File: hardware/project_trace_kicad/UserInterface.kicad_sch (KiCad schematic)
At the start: 13 parts, among them J4 Conn_01x07_Pin, J5 Conn_01x07_Socket, SW1 SW_Push, SW2 SW_Push, SW3 RotaryEncoder, SW4 RotaryEncoder, U1 SBC-OLED01.3

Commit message: Add missing Part-numers, Revise AC Coupling
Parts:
- R1, R2, R3, R4, R5, R6: DigikeyPN (none) -> YAG1236CT-ND
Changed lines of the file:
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@@
+			)
+		)
+		(property "DigikeyPN" "YAG1236CT-ND"
+			(at 195.58 90.17 0)
+			(hide yes)
+			(show_name no)
+			(do_not_autoplace no)
+			(effects
+				(font
+					(size 1.27 1.27)
+				)
 			)
 		)
@@
 			)
 		)
+		(property "DigikeyPN" "YAG1236CT-ND"
+			(at 210.82 115.57 0)
+			(hide yes)
+			(show_name no)
+			(do_not_autoplace no)
+			(effects
+				(font
+					(size 1.27 1.27)
+				)
+			)
+		)
 		(pin "2"
 		)
@@
 			)
 		)
+		(property "DigikeyPN" "YAG1236CT-ND"
+			(at 195.58 36.83 0)
+			(hide yes)
+			(show_name no)
+			(do_not_autoplace no)
+			(effects
+				(font
+					(size 1.27 1.27)
+				)
+			)
+		)
 		(pin "2"
 		)
@@
 			)
 		)
+		(property "DigikeyPN" "YAG1236CT-ND"
+			(at 210.82 143.51 0)
+			(hide yes)
+			(show_name no)
+			(do_not_autoplace no)
+			(effects
+				(font
+					(size 1.27 1.27)
+				)
+			)
+		)
 		(pin "2"
 		)
@@
 			)
 		)
+		(property "DigikeyPN" "YAG1236CT-ND"
+			(at 195.58 74.93 0)
+			(hide yes)
+			(show_name no)
+			(do_not_autoplace no)
+			(effects
+				(font
+					(size 1.27 1.27)
+				)
+			)
+		)
 		(pin "2"
 		)
@@
 			(at 195.58 52.07 0)
 			(hide yes)
+			(show_name no)
+			(do_not_autoplace no)
+			(effects
+				(font
+					(size 1.27 1.27)
+				)
+			)
+		)
+		(property "DigikeyPN" "YAG1236CT-ND"
+			(at 195.58 52.07 0)
+			(hide yes)

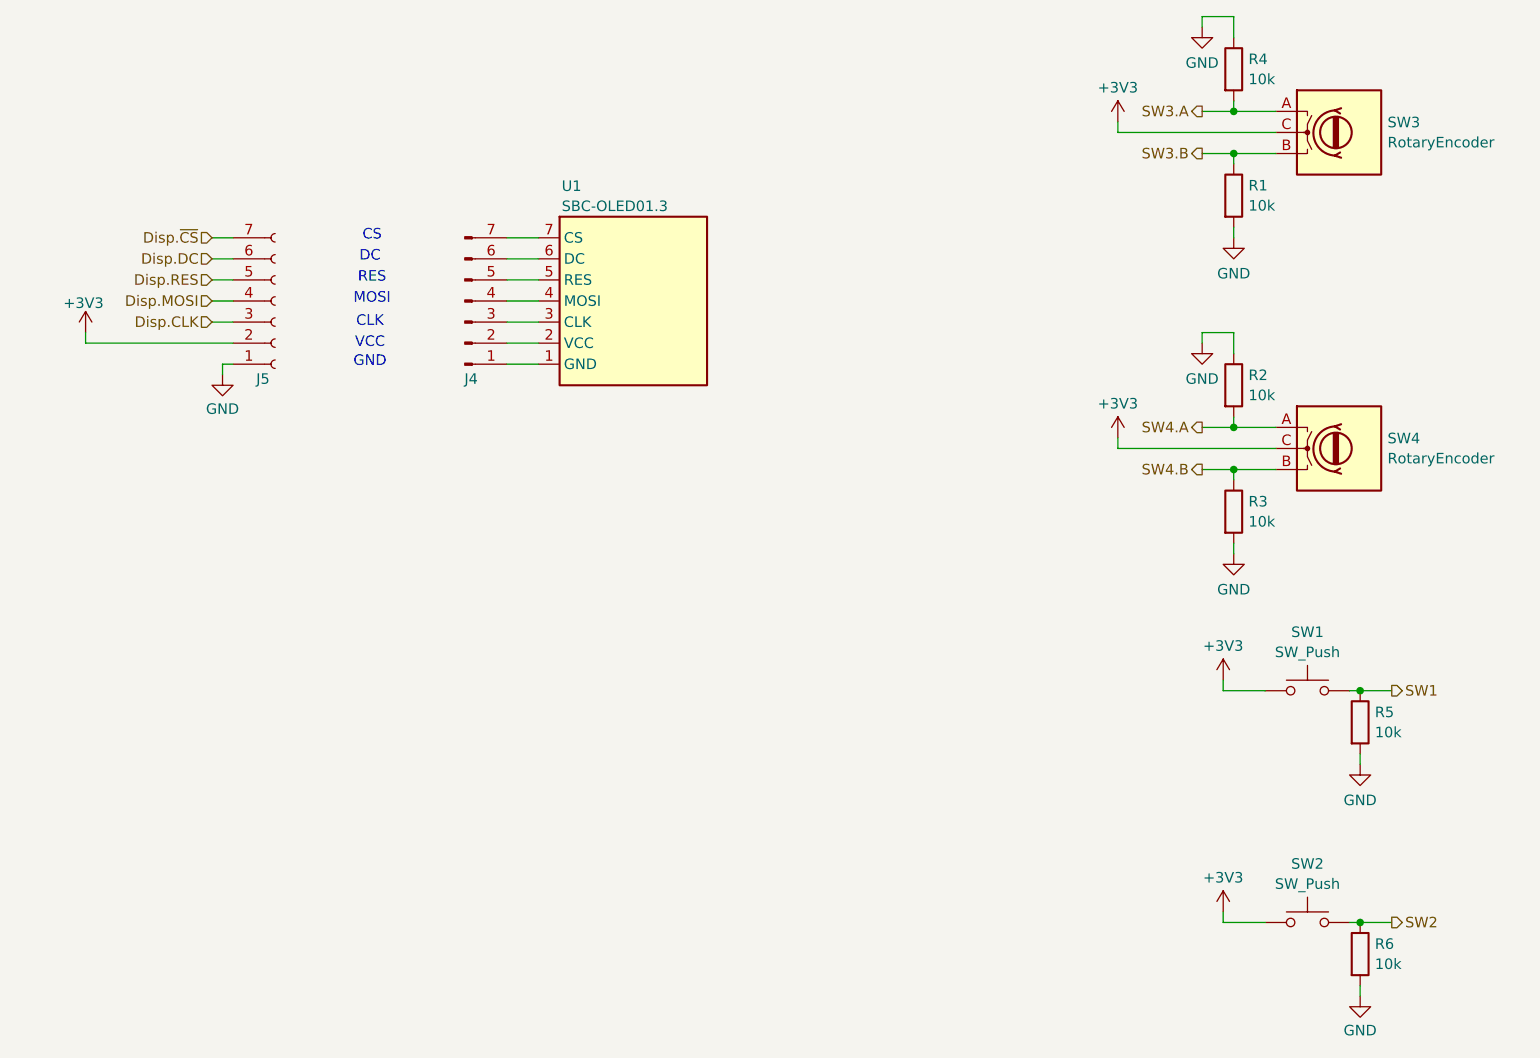
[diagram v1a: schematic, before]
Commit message: UI updated, CLK implemented, Parts labeled as Donotplace in power
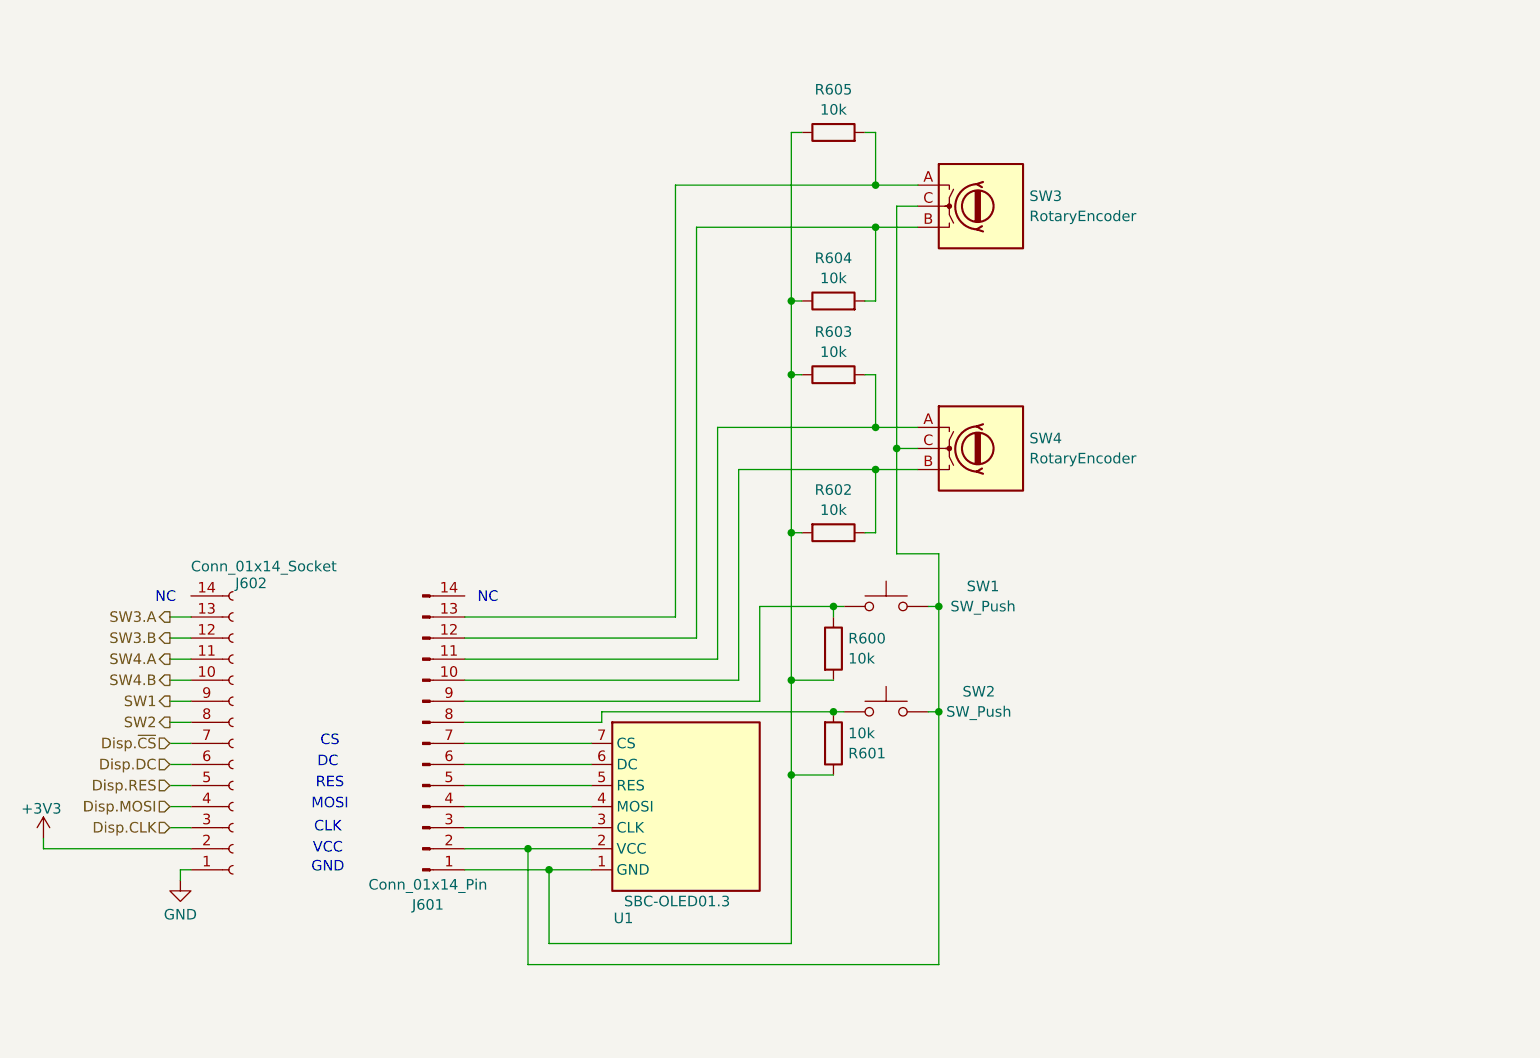
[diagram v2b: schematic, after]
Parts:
- removed J4: Conn_01x07_Pin, symbol Connector:Conn_01x07_Pin
- removed J5: Conn_01x07_Socket, symbol Connector:Conn_01x07_Socket
- removed R1, R2, R3, R4, R6: 10k, symbol Device:R
- added J601: Conn_01x14_Pin, symbol Connector:Conn_01x14_Pin
- added J602: Conn_01x14_Socket, ProjectTraceFootprints:JST_BM14B-GHS-TBT_LF__SN__N_, symbol Connector:Conn_01x14_Socket
- added R601, R602, R603, R604, R605: 10k, Resistor_THT:R_Axial_DIN0207_L6.3mm_D2.5mm_P10.16mm_Horizontal, symbol Device:R
- R600: renamed from R5; footprint (none) -> Resistor_THT:R_Axial_DIN0207_L6.3mm_D2.5mm_P10.16mm_Horizontal
- U1: now in the parts list
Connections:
- net +3V3: now also J602.2 (Pin_2); no longer SW1.1, SW2.1, SW3.C, SW4.C
- net Disp.CLK: now also J602.3 (Pin_3)
- net Disp.DC: now also J602.6 (Pin_6)
- net Disp.MOSI: now also J602.4 (Pin_4)
- net Disp.RES: now also J602.5 (Pin_5)
- net Disp.~{CS}: now also J602.7 (Pin_7)
- net GND: now also J602.1 (Pin_1); no longer R600.2
- net SW1: now also J602.9 (Pin_9); no longer R600.1, SW1.2
- net SW2: now also J602.8 (Pin_8); no longer SW2.2
- net SW3.A: now also J602.13 (Pin_13); no longer SW3.A
- net SW3.B: now also J602.12 (Pin_12); no longer SW3.B
- net SW4.A: now also J602.11 (Pin_11); no longer SW4.A
- net SW4.B: now also J602.10 (Pin_10); no longer SW4.B
- net at U1.1 (GND): now also R600.2, J601.1 (Pin_1), R601.1, R602.2, R603.1, R604.1, R605.1
- net at U1.2 (VCC): now also SW1.2, SW2.1, SW3.C, SW4.C, J601.2 (Pin_2)
- net at U1.3 (CLK): now also J601.3 (Pin_3)
- net at U1.4 (MOSI): now also J601.4 (Pin_4)
- net at U1.5 (RES): now also J601.5 (Pin_5)
- net at U1.6 (DC): now also J601.6 (Pin_6)
- net at U1.7 (CS): now also J601.7 (Pin_7)
- new net: J601.11 (Pin_11), R603.2, SW4.A
- new net: J601.8 (Pin_8), R601.2, SW2.2
- new net: J601.9 (Pin_9), R600.1, SW1.1
- new net: J601.12 (Pin_12), R604.2, SW3.B
- new net: J601.10 (Pin_10), R602.1, SW4.B
- new net: J601.13 (Pin_13), R605.2, SW3.A
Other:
- note added: "NC"
- moved on the sheet: R600, SW1, SW2, SW3, SW4, U1

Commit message: Fix main-merge
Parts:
- renumbered R603 to R3
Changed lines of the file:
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@@
 		(dnp no)
 		(fields_autoplaced yes)
-		(property "Reference" "R603"
+		(property "Reference" "R3"
 			(at 147.32 68.4995 90)
 			(show_name no)
@@
 			(at 147.32 106.68 0)
 			(hide yes)
-			(show_name no)
-			(do_not_autoplace no)
-			(effects
-				(font
-					(size 1.27 1.27)
-				)
-			)
-		)
-		(property "DigikeyPN" "N/A"
-			(at 147.32 106.68 0)
-			(hide yes)
